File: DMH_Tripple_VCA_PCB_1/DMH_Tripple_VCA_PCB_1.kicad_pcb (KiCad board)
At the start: 2 copper layers, 48 x 175 mm, 88 parts, among them J1 TS_Jack_6.35mm_Sw, J10 TS_Jack_6.35mm_Sw, J100 IDC_02x05, J2 TS_Jack_6.35mm_Sw, J200 IDC_02x05, J3 TS_Jack_6.35mm_Sw, J4 TS_Jack_6.35mm_Sw, J5 TS_Jack_6.35mm_Sw, J50 Conn_01x06, J6 TS_Jack_6.35mm_Sw, J60 Conn_01x06, J7 TS_Jack_6.35mm_Sw, J70 Conn_01x06, J8 TS_Jack_6.35mm_Sw, J9 TS_Jack_6.35mm_Sw, Q1 BC548, Q2 BC548, Q3 BC548, Q4 BC548, Q5 BC548, Q6 BC548, U1 TL074, U2 TL074

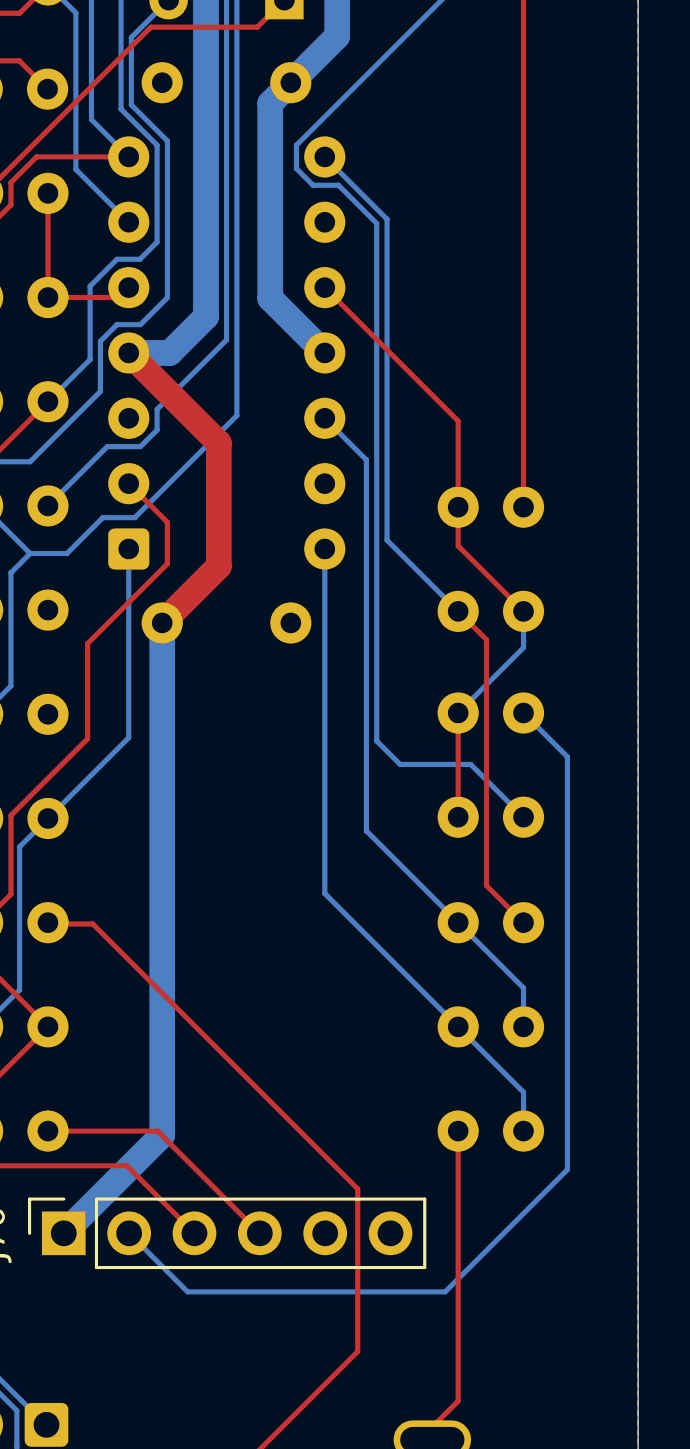
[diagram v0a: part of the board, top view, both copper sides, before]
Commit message: Fixed another mistake
U2C and U2D + and - inputs were inverted
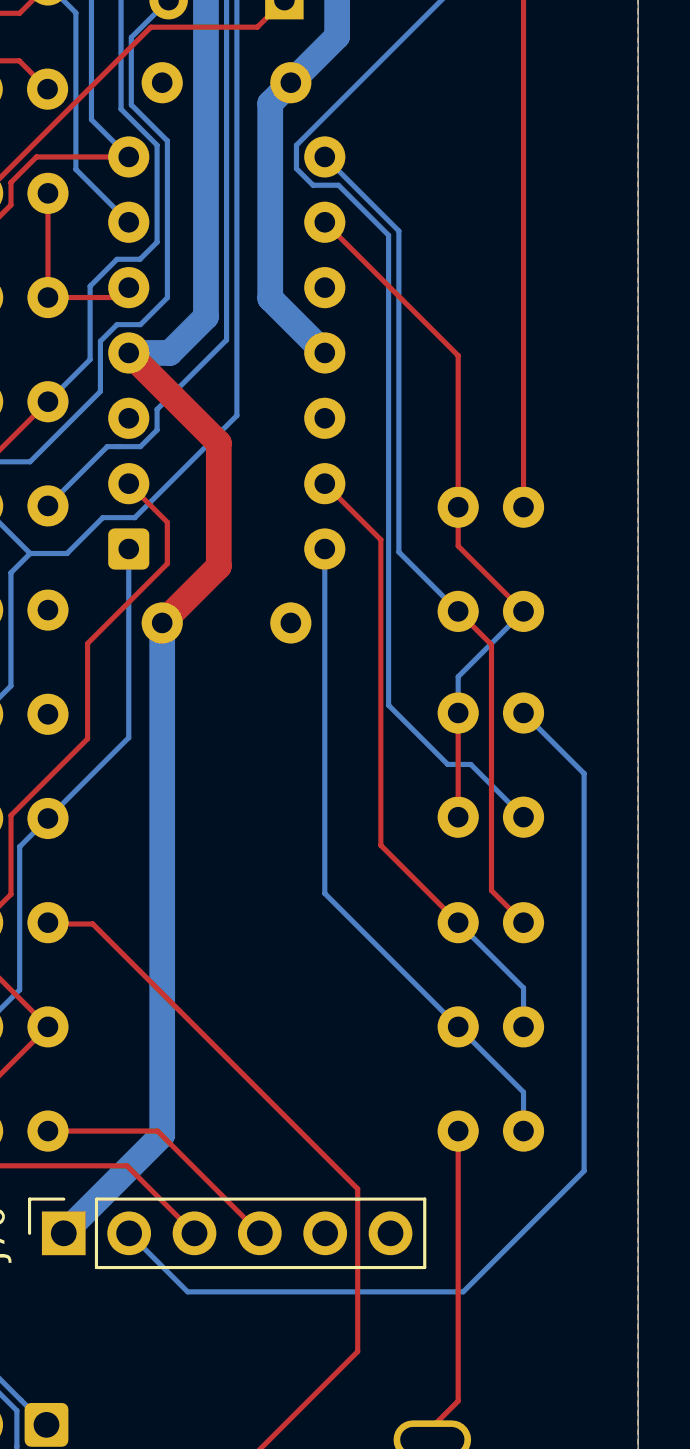
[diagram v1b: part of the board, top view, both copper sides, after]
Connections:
- R46 pad 2: Net-(U2C-+) -> Net-(U2C--)
- R47 pad 1: Net-(U2C-+) -> Net-(U2C--)
- R48 pad 2: Net-(U2C-+) -> Net-(U2C--)
- R49 pad 2: Net-(U2C-+) -> Net-(U2C--)
- R50 pad 2: Net-(U2D-+) -> Net-(U2D--)
- R51 pad 1: Net-(U2D-+) -> Net-(U2D--)
- U2 pad 10: Net-(U2C-+) -> GND
- U2 pad 12: Net-(U2D-+) -> GND
- U2 pad 13: GND -> Net-(U2D--)
- U2 pad 9: GND -> Net-(U2C--)
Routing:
- net Net-(U2C--): track 0.00 -> 27.4 mm
- net Net-(U2D-+): track 26.9 -> 0.00 mm
- net Net-(U2C-+): track 24.8 -> 0.00 mm
- net Net-(U2D--): track 0.00 -> 24.3 mm
- net /Inputs and Outputs/Mute A Switch: track 140.9 -> 139.8 mm
- net /Inputs and Outputs/Mute C Switch: track 38.4 -> 39.3 mm
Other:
- board text added: "Mk1.1 - March 2025"
- board text removed: "Mk1.0 - March 2025"
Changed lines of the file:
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@@
 	(net 59 "Net-(U2B-+)")
 	(net 60 "Net-(R33-Pad1)")
-	(net 61 "Net-(U2D-+)")
+	(net 61 "Net-(U2C--)")
 	(net 62 "Net-(R39-Pad1)")
 	(net 63 "Net-(R42-Pad1)")
@@
 	(net 65 "Net-(U2A--)")
 	(net 66 "Net-(R47-Pad2)")
-	(net 67 "Net-(U2C-+)")
+	(net 67 "Net-(U2D--)")
 	(net 68 "Net-(R51-Pad2)")
 	(footprint "SynthStuff:CUI_MJ-63052A"
@@
 			(layers "*.Cu" "*.Mask")
 			(remove_unused_layers no)
-			(net 67 "Net-(U2C-+)")
+			(net 61 "Net-(U2C--)")
 			(pintype "passive")
 		)
@@
 			(layers "*.Cu" "*.Mask")
 			(remove_unused_layers no)
-			(net 61 "Net-(U2D-+)")
+			(net 67 "Net-(U2D--)")
 			(pintype "passive")
 		)
@@
 			(layers "*.Cu" "*.Mask")
 			(remove_unused_layers no)
-			(net 67 "Net-(U2C-+)")
+			(net 61 "Net-(U2C--)")
 			(pintype "passive")
 		)
@@
 			(layers "*.Cu" "*.Mask")
 			(remove_unused_layers no)
-			(net 67 "Net-(U2C-+)")
+			(net 61 "Net-(U2C--)")
 			(pintype "passive")
 		)
@@
 			(layers "*.Cu" "*.Mask")
 			(remove_unused_layers no)
-			(net 67 "Net-(U2C-+)")
+			(net 61 "Net-(U2C--)")
 			(pintype "passive")
 		)
@@
 			(layers "*.Cu" "*.Mask")
 			(remove_unused_layers no)
-			(net 61 "Net-(U2D-+)")
+			(net 67 "Net-(U2D--)")
 			(pintype "passive")
 		)
@@
 			(layers "*.Cu" "*.Mask")
 			(remove_unused_layers no)
-			(net 2 "GND")
+			(net 61 "Net-(U2C--)")
 			(pinfunction "-")
 			(pintype "input")
@@
 			(layers "*.Cu" "*.Mask")
 			(remove_unused_layers no)
-			(net 67 "Net-(U2C-+)")
+			(net 2 "GND")
 			(pinfunction "+")
 			(pintype "input")
@@
 			(layers "*.Cu" "*.Mask")
 			(remove_unused_layers no)
-			(net 61 "Net-(U2D-+)")
+			(net 2 "GND")
 			(pinfunction "+")
 			(pintype "input")
@@
 			(layers "*.Cu" "*.Mask")
 			(remove_unused_layers no)
-			(net 2 "GND")
+			(net 67 "Net-(U2D--)")
 			(pinfunction "-")
 			(pintype "input")
@@
 		(layer "User.9")
 	)
-	(gr_text "Mk1.0 - March 2025"
+	(gr_text "Mk1.1 - March 2025"
 		(at 59.55 216.25 0)
 		(layer "B.SilkS")
@@
 	)
 	(segment
-		(start 88.839 154.9711)
-		(end 87.3539 153.486)
+		(start 83.94 66.25)
+		(end 79.215 70.975)
 		(width 0.2)
 		(layer "B.Cu")
@@
 	)
 	(segment
-		(start 86.36395 153.486)
-		(end 85.719 152.84105)
+		(start 85.719 151.92895)
+		(end 97 140.64795)
 		(width 0.2)
 		(layer "B.Cu")
@@
 	)
 	(segment
-		(start 85.719 151.92895)
-		(end 97 140.64795)
+		(start 97 68.25)
+		(end 95 66.25)
 		(width 0.2)
 		(layer "B.Cu")
@@
 	)
 	(segment
-		(start 95 66.25)
-		(end 83.94 66.25)
+		(start 89.3 155.4321)
+		(end 87.3539 153.486)
 		(width 0.2)
 		(layer "B.Cu")
@@
 	(segment
 		(start 92.495 176)
-		(end 89.75 176)
+		(end 91.6 176)
 		(width 0.2)
 		(layer "B.Cu")
@@
 	)
 	(segment
-		(start 88.839 175.089)
-		(end 88.839 154.9711)
+		(start 95 66.25)
+		(end 83.94 66.25)
 		(width 0.2)
 		(layer "B.Cu")
@@
 	)
 	(segment
-		(start 83.94 66.25)
-		(end 79.215 70.975)
+		(start 87.3539 153.486)
+		(end 86.36395 153.486)
 		(width 0.2)
 		(layer "B.Cu")
@@
 	)
 	(segment
-		(start 94.545 178.05)
-		(end 92.495 176)
+		(start 86.36395 153.486)
+		(end 85.719 152.84105)
 		(width 0.2)
 		(layer "B.Cu")
@@
 	)
 	(segment
-		(start 85.719 152.84105)
-		(end 85.719 151.92895)
+		(start 91.6 176)
+		(end 89.3 173.7)
 		(width 0.2)
 		(layer "B.Cu")
@@
 	)
 	(segment
-		(start 97 68.25)
-		(end 95 66.25)
+		(start 94.545 178.05)
+		(end 92.495 176)
 		(width 0.2)
 		(layer "B.Cu")
@@
 	)
 	(segment
-		(start 87.3539 153.486)
-		(end 86.36395 153.486)
+		(start 85.719 152.84105)
+		(end 85.719 151.92895)
 		(width 0.2)
 		(layer "B.Cu")
@@
 	)
 	(segment
-		(start 89.75 176)
-		(end 88.839 175.089)
+		(start 89.3 173.7)
+		(end 89.3 155.4321)
 		(width 0.2)
 		(layer "B.Cu")
@@
 	)
 	(segment
-		(start 96.25 191.75)
-		(end 91.5 196.5)
+		(start 92.2 196.5)
+		(end 81.49 196.5)
 		(width 0.2)
 		(layer "B.Cu")
@@
 	)
 	(segment
-		(start 91.5 196.5)
-		(end 81.49 196.5)
+		(start 96.9 176.355)
+		(end 96.9 191.8)
 		(width 0.2)
 		(layer "B.Cu")
@@
 	)
 	(segment
-		(start 96.25 175.705)
-		(end 96.25 191.75)
+		(start 96.9 191.8)
+		(end 92.2 196.5)
 		(width 0.2)
 		(layer "B.Cu")
@@
 	(segment
 		(start 94.545 174)
-		(end 96.25 175.705)
+		(end 96.9 176.355)
 		(width 0.2)
 		(layer "B.Cu")
@@
 	)
 	(segment
-		(start 92.005 182.15)
-		(end 88.438 178.583)
+		(start 92.005 166)
+		(end 92.005 167.51)
 		(width 0.2)
-		(layer "B.Cu")
+		(layer "F.Cu")
 		(net 61)
 	)
 	(segment
-		(start 88.438 164.163)
-		(end 86.82 162.545)
+		(start 92.005 178.05)
+		(end 92.005 174)
 		(width 0.2)
-		(layer "B.Cu")
+		(layer "F.Cu")
 		(net 61)
 	)
 	(segment
-		(start 88.438 178.583)
-		(end 88.438 164.163)
+		(start 92.005 160.11)
+		(end 86.82 154.925)
 		(width 0.2)
-		(layer "B.Cu")
+		(layer "F.Cu")
 		(net 61)
 	)
 	(segment
-		(start 94.545 186.2)
-		(end 94.545 184.69)
+		(start 92.005 167.51)
+		(end 94.545 170.05)
+		(width 0.2)
+		(layer "F.Cu")
+		(net 61)
+	)
+	(segment
+		(start 92.005 166)
+		(end 92.005 160.11)
+		(width 0.2)
+		(layer "F.Cu")
+		(net 61)
+	)
+	(segment
+		(start 92.005 172.59)
+		(end 94.545 170.05)
 		(width 0.2)
 		(layer "B.Cu")
@@
 	)
 	(segment
-		(start 94.545 184.69)
-		(end 92.005 182.15)
+		(start 92.005 174)
+		(end 92.005 172.59)
 		(width 0.2)
 		(layer "B.Cu")
@@
 	)
 	(segment
-		(start 93.106 171.151)
-		(end 93.106 180.711)
+		(start 92.005 170.05)
+		(end 93.3 171.345)
 		(width 0.2)
 		(layer "F.Cu")
@@
 	)
 	(segment
-		(start 93.106 180.711)
-		(end 94.545 182.15)
+		(start 93.3 171.345)
+		(end 93.3 180.905)
 		(width 0.2)
 		(layer "F.Cu")
@@
 	)
 	(segment
-		(start 92.005 170.05)
-		(end 93.106 171.151)
+		(start 93.3 180.905)
+		(end 94.545 182.15)
 		(width 0.2)
 		(layer "F.Cu")
@@
 	(segment
 		(start 86.82 152.385)
-		(end 89.24 154.805)
+		(end 89.7 155.265)
 		(width 0.2)
 		(layer "B.Cu")
@@
 	)
 	(segment
-		(start 89.24 154.805)
-		(end 89.24 167.285)
+		(start 89.7 167.745)
+		(end 92.005 170.05)
 		(width 0.2)
 		(layer "B.Cu")
@@
 	)
 	(segment
-		(start 89.24 167.285)
-		(end 92.005 170.05)
+		(start 89.7 155.265)
+		(end 89.7 167.745)
 		(width 0.2)
 		(layer "B.Cu")
@@
 	)
 	(segment
-		(start 92.005 166)
-		(end 92.005 167.51)
-		(width 0.2)
-		(layer "F.Cu")
-		(net 67)
-	)
-	(segment
-		(start 92.005 162.65)
-		(end 92.005 166)
-		(width 0.2)
-		(layer "F.Cu")
-		(net 67)
-	)
-	(segment
-		(start 92.005 178.05)
-		(end 92.005 174)
+		(start 89 179.145)
+		(end 89 167.265)
 		(width 0.2)
 		(layer "F.Cu")
@@
 	)
 	(segment
-		(start 92.005 167.51)
-		(end 94.545 170.05)
+		(start 92.005 182.15)
+		(end 89 179.145)
 		(width 0.2)
 		(layer "F.Cu")
@@
 	)
 	(segment
-		(start 86.82 157.465)
-		(end 92.005 162.65)
+		(start 89 167.265)
+		(end 86.82 165.085)
 		(width 0.2)
 		(layer "F.Cu")
@@
 	)
 	(segment
-		(start 94.545 171.46)
-		(end 92.005 174)
+		(start 94.545 186.2)
+		(end 94.545 184.69)
 		(width 0.2)
 		(layer "B.Cu")
@@
 	)
 	(segment
-		(start 94.545 170.05)
-		(end 94.545 171.46)
+		(start 94.545 184.69)
+		(end 92.005 182.15)
 		(width 0.2)
 		(layer "B.Cu")
